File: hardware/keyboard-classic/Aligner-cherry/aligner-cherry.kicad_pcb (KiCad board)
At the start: 2 copper layers, 312.4 x 118.1 mm, 74 parts, among them SW1 RT Arrow, SW10 Bracket_Open, SW11 6, SW12 Y, SW13 Return, SW14 Dash, SW15 5, SW16 T, SW17 Line Feed, SW18 Colon, SW19 4, SW2 LT Arrow, SW20 R, SW21 O, SW22 0, SW23 3, SW24 E, SW25 L, SW26 9, SW27 2, SW28 W, SW29 Period, SW3 Tilde, SW30 8, SW31 1, SW32 @ (AT), SW33 Break, SW34 Rubout, SW35 R_Shift, SW36 P, SW37 Comma, SW38 K, SW39 L_Shift, SW4 I, SW40 Semicolon, SW41 M, SW42 J, SW43 Fwd_Slash, SW44 N, SW45 H, SW46 SPACE, SW47 B, SW48 G, SW49 TAB, SW5 Repeat, SW50 Z, SW51 V, SW52 F, SW53 CTRL, SW54 A, SW55 C, SW56 D, SW57 Backslash, SW58 Q, SW59 X, SW6 Bracket_Close, SW60 S, SW61 FN, SW62 ESC, SW7 7, SW8 U, SW9 Caps Lock

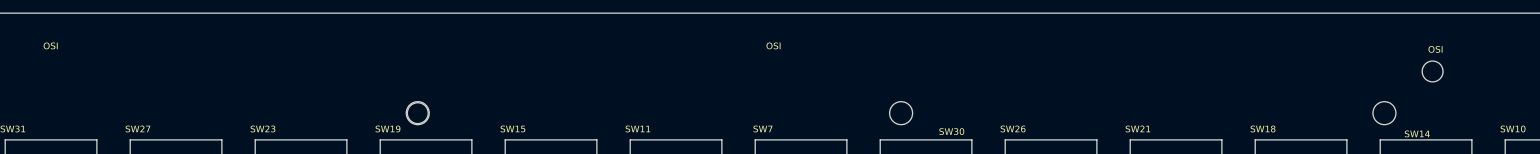
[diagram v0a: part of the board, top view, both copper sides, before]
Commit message: Replaced standard 20-pin header with header+mounting holes
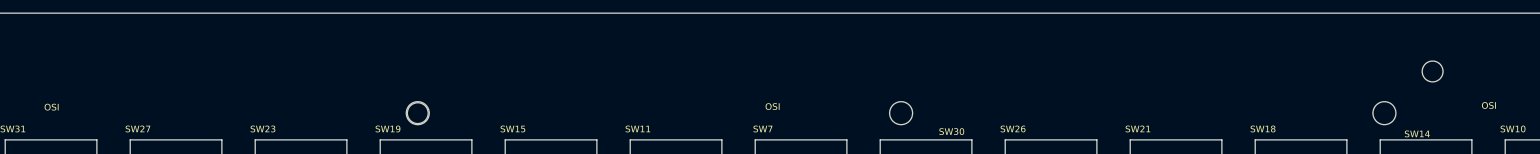
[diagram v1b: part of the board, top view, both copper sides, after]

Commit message: 0.05" adjustment to position of top mounting holes to match pcb
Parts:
- removed the REF** at (143.5, 78.7)
- removed the REF** at (364.5, 78.7)
- removed the REF** at (290.8, 78.7)
- added REF**: MountingHole_3.5mm, MountingHole:MountingHole_3.5mm, F.Cu at (143.5, 77.5)
- added REF**: MountingHole_3.5mm, MountingHole:MountingHole_3.5mm, F.Cu at (364.5, 77.5)
- added REF**: MountingHole_3.5mm, MountingHole:MountingHole_3.5mm, F.Cu at (290.8, 77.5)
- moved REF** 1.27 mm to (67.3, 77.5)
- moved REF** 1.27 mm to (217.2, 77.5)

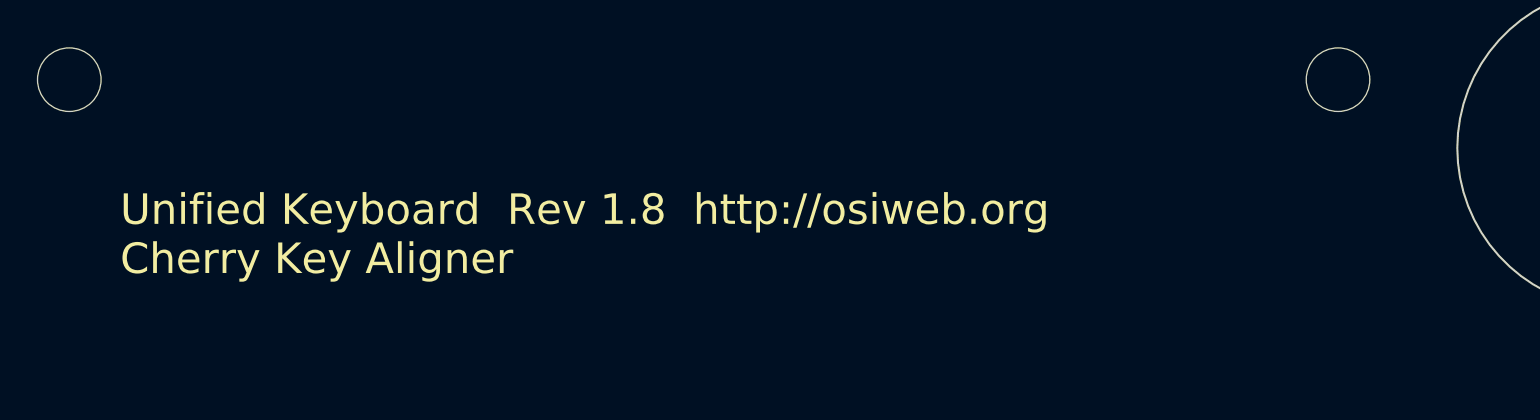
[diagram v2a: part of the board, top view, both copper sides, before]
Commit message: Add BOM parameter fields to apple2 and 328P encoders and classic kbd
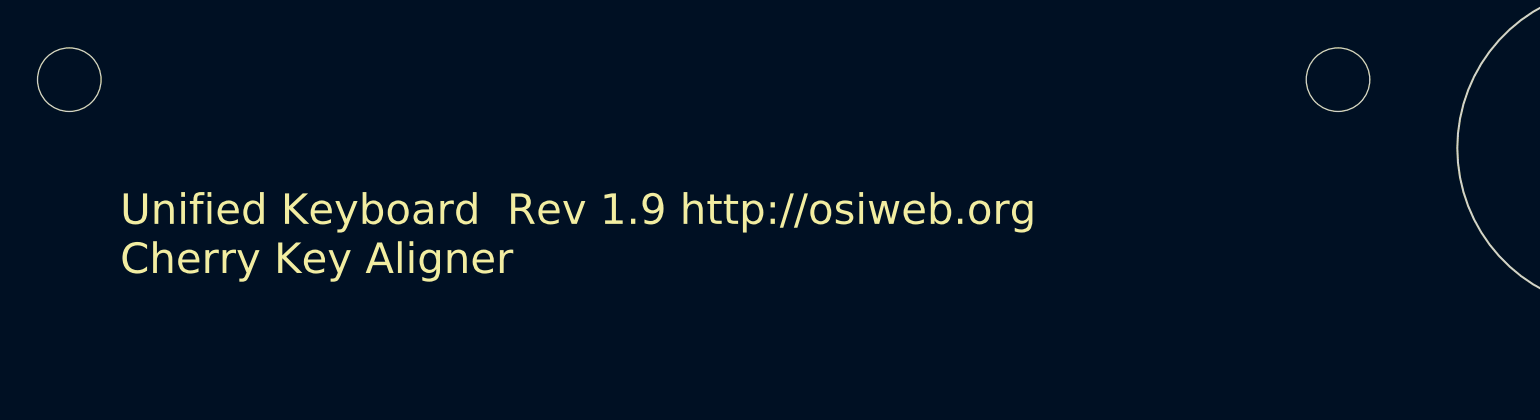
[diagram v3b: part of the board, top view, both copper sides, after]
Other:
- board text added: "Unified Keyboard Rev 1.9 http://osiweb.org Cherry Key Aligner"
- board text removed: "Unified Keyboard Rev 1.8 http://osiweb.org Cherry Key Aligner"

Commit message: Multiple fixes for keyboard PCB
- in combined CherryMX/futaba footprints, moved cherry pads down 1 mil and
futaba pads up 2 mil, to reduce risk of shortin of LED pads with futaba pad.
Adjusted all aligners accordingly

- Fixed centroid for combined diode footprint and adjusted PCB placement on
classic and SOL keyboards accordingly.

- Moved SMT pads in combined diode footprint to top layer, so pick & place file
will be usable.

- changes to futaba stabilizer design.  Longer post adapter passes through slots
in keyboard and aligner.

- Changed futaba post thickness gauge from board outline to a slot to improve
tolerance.

- Moved spacebar stabilizer bending guide to edge of PCB, in order to make it
more useful in bending PCBs.

- Changed Apple II mounting slots on classic keyboard from horizontal to
vertical orientation, to accommodate the different spacing offets due to the use
of spacers in angled mounting threads.
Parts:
- removed SW46: SPACE, unikbd:MX_space_aligner
- added REF**: MX_space_aligner, unikbd:MX_space_aligner, F.Cu at (197.2, 166.0)
- moved REF** 27.5 mm to (236.2, 177.8)
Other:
- outline, holes or cut-outs redrawn
- board text added: "Unified Keyboard Rev 1.10 http://osiweb.org Cherry Key Aligner"
- board text removed: "Stabilzer bend guide"
- board text removed: "Unified Keyboard Rev 1.9 http://osiweb.org Cherry Key Aligner"

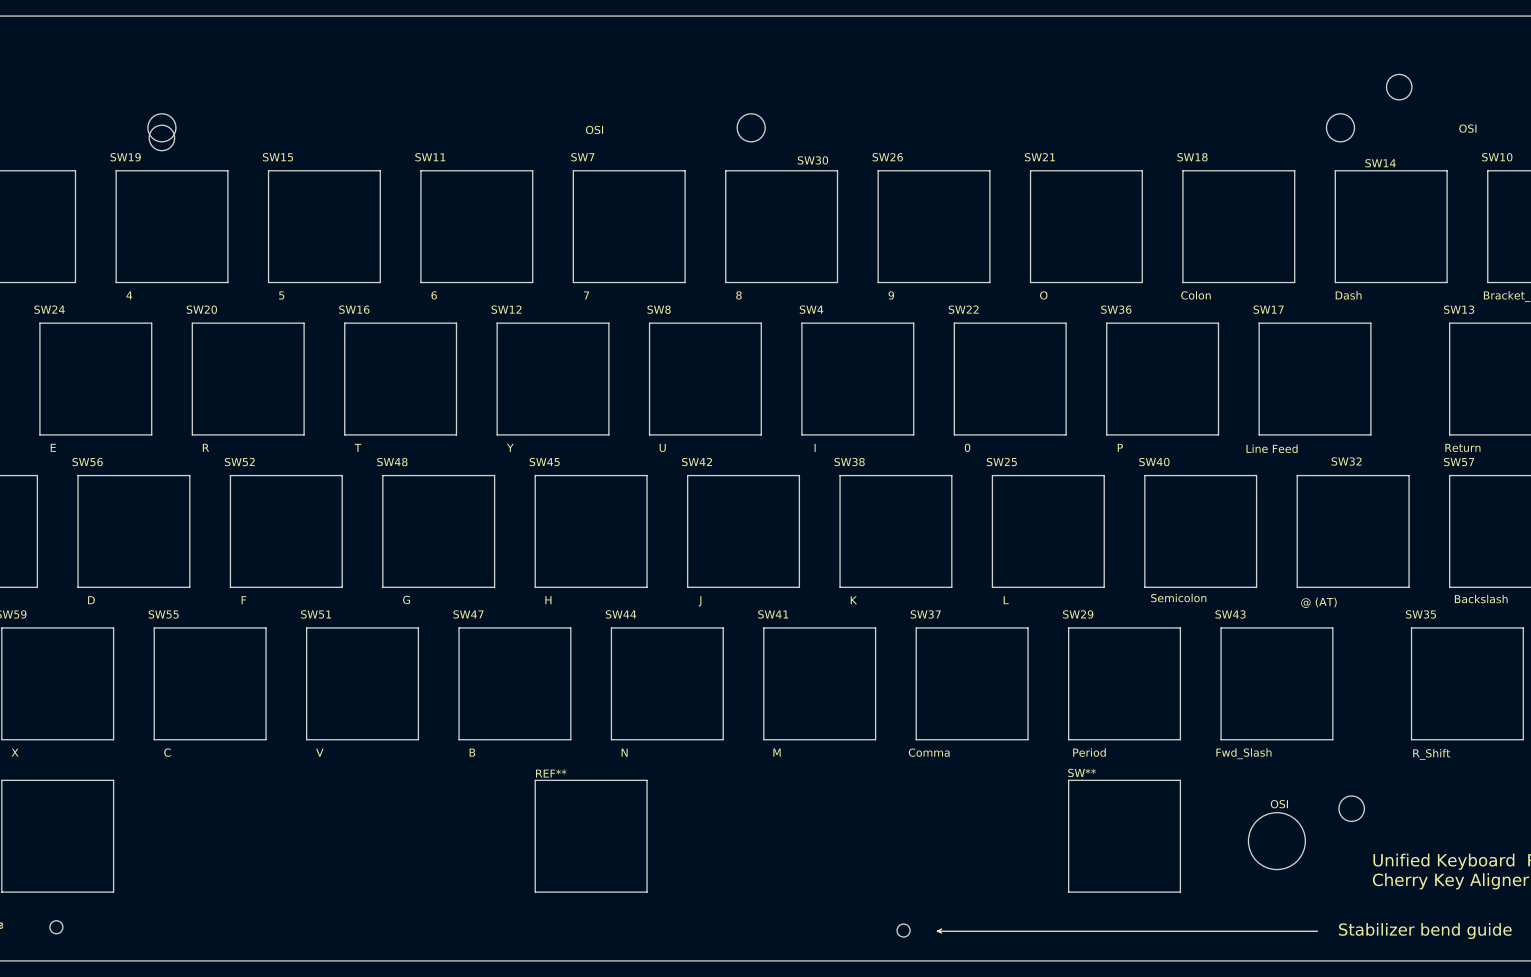
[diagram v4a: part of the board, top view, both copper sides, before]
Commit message: Apply fixes to cherry aligner.
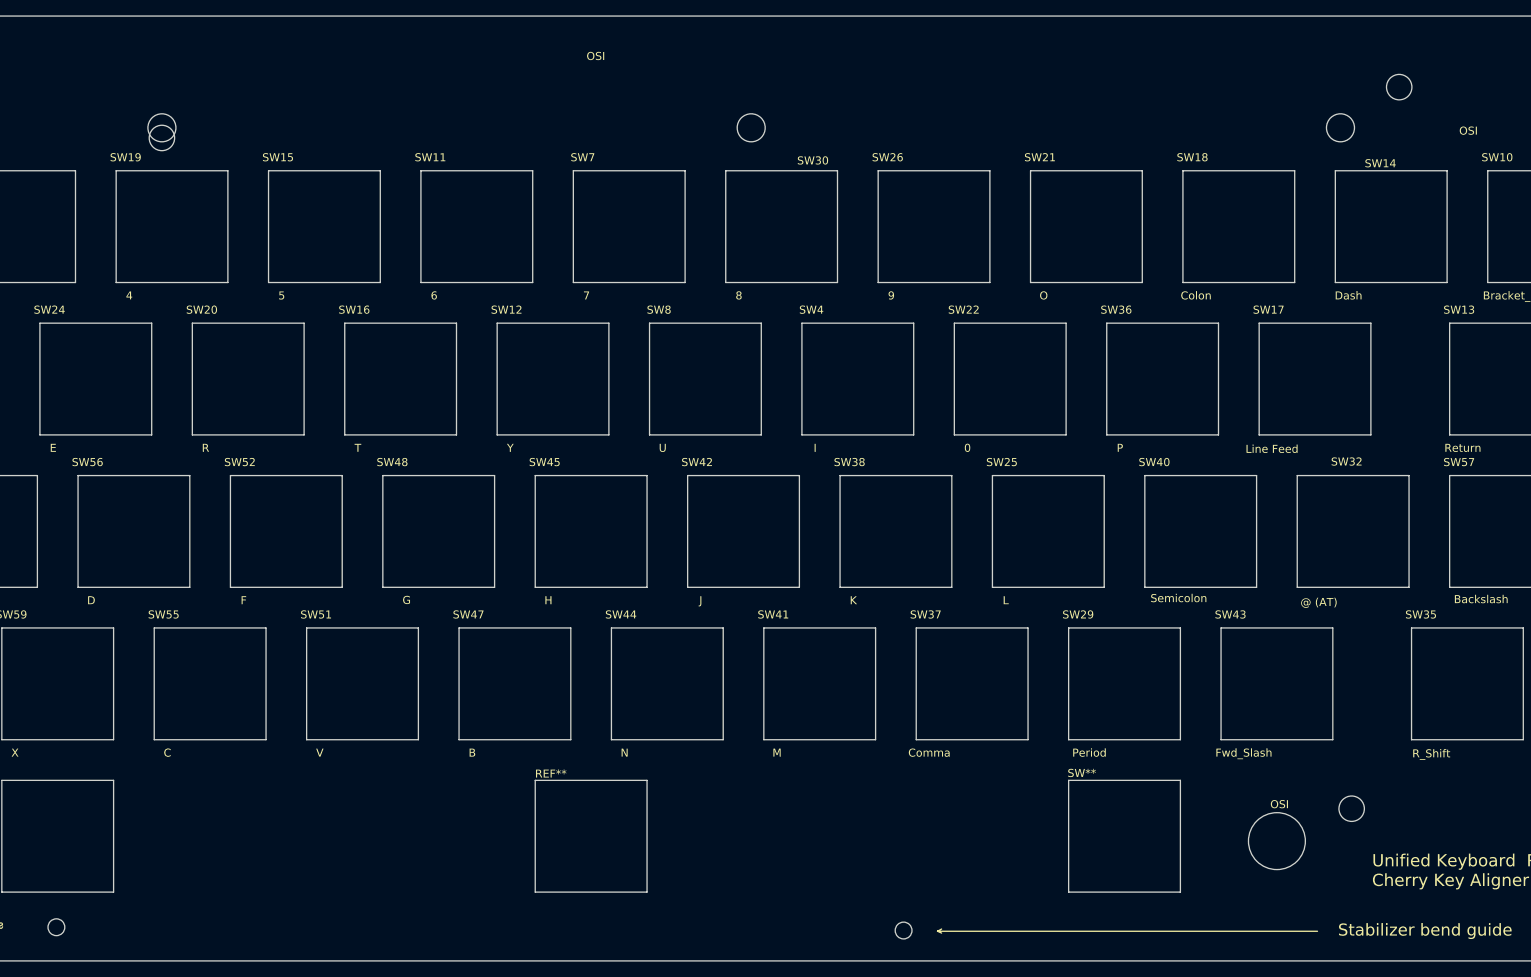
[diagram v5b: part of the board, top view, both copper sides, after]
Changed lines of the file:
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@@
+      (effects (font (size 1 1) (thickness 0.15)))
+    )
+    (fp_text user %R (at 110.75162 -87.97036) (layer F.Fab)
+      (effects (font (size 1 1) (thickness 0.15)))
+    )
+    (fp_text user OSI (at -109.4232 -88.138) (layer F.SilkS)
+      (effects (font (size 1 1) (thickness 0.15)))
+    )
+    (fp_text user %R (at -85.03158 5.42544) (layer F.Fab)
+      (effects (font (size 1 1) (thickness 0.15)))
+    )
+    (fp_text user OSI (at -85.28558 -4.17576) (layer F.SilkS)
+      (effects (font (size 1 1) (thickness 0.15)))
+    )
+    (fp_text user %R (at 86.31682 5.65404) (layer F.Fab)
+      (effects (font (size 1 1) (thickness 0.15)))
+    )
+    (fp_text user OSI (at 86.06282 -3.94716) (layer F.SilkS)
+      (effects (font (size 1 1) (thickness 0.15)))
+    )
+    (fp_text user OSI (at 0.59182 -97.46996) (layer F.SilkS)
+      (effects (font (size 1 1) (thickness 0.15)))
+    )
+    (fp_text user %R (at 0.84582 -87.86876) (layer F.Fab)
+      (effects (font (size 1 1) (thickness 0.15)))
+    )
+    (fp_text user OSI (at -109.4232 -88.138) (layer F.SilkS)
+      (effects (font (size 1 1) (thickness 0.15)))
+    )
+    (fp_text user %R (at -109.31398 -87.86876) (layer F.Fab)
+      (effects (font (size 1 1) (thickness 0.15)))
+    )
+    (fp_text user OSI (at 109.6772 -88.138) (layer F.SilkS)
+      (effects (font (size 1 1) (thickness 0.15)))
+    )
+    (fp_text user %R (at 110.75162 -87.97036) (layer F.Fab)
       (effects (font (size 1 1) (thickness 0.15)))
     )
@@
     (fp_circle (center -109.22 -92.71) (end -104.394 -92.71) (layer Cmts.User) (width 0.15))
     (fp_circle (center 109.22 -92.71) (end 114.046 -92.71) (layer Cmts.User) (width 0.15))
-    (fp_text user %R (at 110.75162 -87.97036) (layer F.Fab)
-      (effects (font (size 1 1) (thickness 0.15)))
-    )
-    (fp_text user OSI (at 109.6264 -88.392) (layer F.SilkS)
-      (effects (font (size 1 1) (thickness 0.15)))
-    )
-    (fp_text user %R (at -85.03158 5.42544) (layer F.Fab)
-      (effects (font (size 1 1) (thickness 0.15)))
-    )
-    (fp_text user OSI (at -85.28558 -4.17576) (layer F.SilkS)
-      (effects (font (size 1 1) (thickness 0.15)))
-    )
-    (fp_text user %R (at 86.31682 5.65404) (layer F.Fab)
-      (effects (font (size 1 1) (thickness 0.15)))
-    )
-    (fp_text user OSI (at 86.06282 -3.94716) (layer F.SilkS)
-      (effects (font (size 1 1) (thickness 0.15)))
-    )
-    (fp_text user OSI (at 0.45212 -88.22436) (layer F.SilkS)
-      (effects (font (size 1 1) (thickness 0.15)))
-    )
-    (fp_text user %R (at 0.84582 -87.86876) (layer F.Fab)
-      (effects (font (size 1 1) (thickness 0.15)))
-    )
-    (fp_text user OSI (at -109.4232 -88.138) (layer F.SilkS)
-      (effects (font (size 1 1) (thickness 0.15)))
-    )
-    (fp_text user %R (at -109.31398 -87.86876) (layer F.Fab)
-      (effects (font (size 1 1) (thickness 0.15)))
-    )
-    (fp_text user %R (at 110.75162 -87.97036) (layer F.Fab)
-      (effects (font (size 1 1) (thickness 0.15)))
-    )
     (pad "" np_thru_hole circle (at -85.725 0.635) (size 7.112 7.112) (drill 7.112) (layers *.Cu *.Mask))
     (pad "" np_thru_hole circle (at 85.725 0.635) (size 7.112 7.112) (drill 7.112) (layers *.Cu *.Mask))
@@
       (effects (font (size 1 1) (thickness 0.15)))
     )
-    (pad "" np_thru_hole circle (at 0 0) (size 1.6256 1.6256) (drill 1.6256) (layers *.Cu *.Mask))
+    (fp_text user %R (at 0.3 0) (layer F.Fab)
+      (effects (font (size 1 1) (thickness 0.15)))
+    )
+    (fp_circle (center 0 0) (end 2.1 0) (layer Cmts.User) (width 0.15))
+    (fp_circle (center 0 0) (end 2.35 0) (layer F.CrtYd) (width 0.05))
+    (pad "" np_thru_hole circle (at 0 0) (size 2.1 2.1) (drill 2.1) (layers *.Cu *.Mask))
   )
   (module MountingHole:MountingHole_2.1mm (layer F.Cu)
@@
       (effects (font (size 1 1) (thickness 0.15)))
     )
-    (pad "" np_thru_hole circle (at 0 0) (size 1.6256 1.6256) (drill 1.6256) (layers *.Cu *.Mask))
+    (fp_text user %R (at 0.3 0) (layer F.Fab)
+      (effects (font (size 1 1) (thickness 0.15)))
+    )
+    (fp_circle (center 0 0) (end 2.1 0) (layer Cmts.User) (width 0.15))
+    (fp_circle (center 0 0) (end 2.35 0) (layer F.CrtYd) (width 0.05))
+    (pad "" np_thru_hole circle (at 0 0) (size 2.1 2.1) (drill 2.1) (layers *.Cu *.Mask))
   )
   (module Symbol:OSHW-Logo2_9.8x8mm_SilkScreen (layer F.Cu)
@@
       (effects (font (size 1 1) (thickness 0.15)))
     )
-    (fp_circle (center 0 0) (end 3.5 0) (layer Cmts.User) (width 0.15))
-    (fp_circle (center 0 0) (end 3.75 0) (layer F.CrtYd) (width 0.05))
-    (fp_text user %R (at 0.3 0) (layer F.Fab) hide
-      (effects (font (size 1 1) (thickness 0.15)))
-    )
+    (fp_text user %R (at 0.3 0) (layer F.Fab) hide
+      (effects (font (size 1 1) (thickness 0.15)))
+    )
+    (fp_circle (center 0 0) (end 3.5 0) (layer Cmts.User) (width 0.15))
+    (fp_circle (center 0 0) (end 3.75 0) (layer F.CrtYd) (width 0.05))
     (pad 1 np_thru_hole circle (at 0 0) (size 3.5 3.5) (drill 3.5) (layers *.Cu *.Mask))
   )
@@
       (effects (font (size 1 1) (thickness 0.15)))
     )
-    (fp_circle (center 0 0) (end 3.75 0) (layer F.CrtYd) (width 0.05))
-    (fp_circle (center 0 0) (end 3.5 0) (layer Cmts.User) (width 0.15))
-    (fp_text user %R (at 0.3 0) (layer F.Fab) hide
-      (effects (font (size 1 1) (thickness 0.15)))
-    )
+    (fp_text user %R (at 0.3 0) (layer F.Fab) hide
+      (effects (font (size 1 1) (thickness 0.15)))
+    )
+    (fp_circle (center 0 0) (end 3.5 0) (layer Cmts.User) (width 0.15))
+    (fp_circle (center 0 0) (end 3.75 0) (layer F.CrtYd) (width 0.05))
     (pad 1 np_thru_hole circle (at 0 0) (size 3.5 3.5) (drill 3.5) (layers *.Cu *.Mask))
   )
@@
       (effects (font (size 1 1) (thickness 0.15)))
     )
-    (fp_circle (center 0 0) (end 3.75 0) (layer F.CrtYd) (width 0.05))
-    (fp_circle (center 0 0) (end 3.5 0) (layer Cmts.User) (width 0.15))
-    (fp_text user %R (at 0.3 0) (layer F.Fab) hide
-      (effects (font (size 1 1) (thickness 0.15)))
-    )
+    (fp_text user %R (at 0.3 0) (layer F.Fab) hide
+      (effects (font (size 1 1) (thickness 0.15)))
+    )
+    (fp_circle (center 0 0) (end 3.5 0) (layer Cmts.User) (width 0.15))
+    (fp_circle (center 0 0) (end 3.75 0) (layer F.CrtYd) (width 0.05))
     (pad 1 np_thru_hole circle (at 0 0) (size 3.5 3.5) (drill 3.5) (layers *.Cu *.Mask))
   )
@@
       (effects (font (size 1 1) (thickness 0.15)))
     )
-    (fp_circle (center 0 0) (end 3.75 0) (layer F.CrtYd) (width 0.05))
-    (fp_circle (center 0 0) (end 3.5 0) (layer Cmts.User) (width 0.15))
-    (fp_text user %R (at 0.3 0) (layer F.Fab) hide
-      (effects (font (size 1 1) (thickness 0.15)))
-    )
+    (fp_text user %R (at 0.3 0) (layer F.Fab) hide
+      (effects (font (size 1 1) (thickness 0.15)))
+    )
+    (fp_circle (center 0 0) (end 3.5 0) (layer Cmts.User) (width 0.15))
+    (fp_circle (center 0 0) (end 3.75 0) (layer F.CrtYd) (width 0.05))
     (pad 1 np_thru_hole circle (at 0 0) (size 3.5 3.5) (drill 3.5) (layers *.Cu *.Mask))
   )
@@
       (effects (font (size 1 1) (thickness 0.15)))
     )
-    (fp_circle (center 0 0) (end 3.75 0) (layer F.CrtYd) (width 0.05))
-    (fp_circle (center 0 0) (end 3.5 0) (layer Cmts.User) (width 0.15))
-    (fp_text user %R (at 0.3 0) (layer F.Fab) hide
-      (effects (font (size 1 1) (thickness 0.15)))
-    )
+    (fp_text user %R (at 0.3 0) (layer F.Fab) hide
+      (effects (font (size 1 1) (thickness 0.15)))
+    )
+    (fp_circle (center 0 0) (end 3.5 0) (layer Cmts.User) (width 0.15))
+    (fp_circle (center 0 0) (end 3.75 0) (layer F.CrtYd) (width 0.05))
     (pad 1 np_thru_hole circle (at 0 0) (size 3.5 3.5) (drill 3.5) (layers *.Cu *.Mask))
   )
@@
       (effects (font (size 1 1) (thickness 0.15)))
     )
-    (fp_circle (center 0 0) (end 3.75 0) (layer F.CrtYd) (width 0.05))
-    (fp_circle (center 0 0) (end 3.5 0) (layer Cmts.User) (width 0.15))
-    (fp_text user %R (at 0.3 0) (layer F.Fab) hide
-      (effects (font (size 1 1) (thickness 0.15)))
-    )
+    (fp_text user %R (at 0.3 0) (layer F.Fab) hide
+      (effects (font (size 1 1) (thickness 0.15)))
+    )
+    (fp_circle (center 0 0) (end 3.5 0) (layer Cmts.User) (width 0.15))
+    (fp_circle (center 0 0) (end 3.75 0) (layer F.CrtYd) (width 0.05))
     (pad 1 np_thru_hole circle (at 0 0) (size 3.5 3.5) (drill 3.5) (layers *.Cu *.Mask))
   )
@@
       (effects (font (size 1 1) (thickness 0.15)))
     )
-    (fp_circle (center 0 0) (end 3.75 0) (layer F.CrtYd) (width 0.05))
-    (fp_circle (center 0 0) (end 3.5 0) (layer Cmts.User) (width 0.15))
-    (fp_text user %R (at 0.3 0) (layer F.Fab) hide
-      (effects (font (size 1 1) (thickness 0.15)))
-    )
-    (pad 1 np_thru_hole circle (at 0 0) (size 3.5 3.5) (drill 3.5) (layers *.Cu *.Mask))
-  )
+    (fp_text user %R (at 0.3 0) (layer F.Fab) hide
+      (effects (font (size 1 1) (thickness 0.15)))
+    )
+    (fp_circle (center 0 0) (end 3.5 0) (layer Cmts.User) (width 0.15))
+    (fp_circle (center 0 0) (end 3.75 0) (layer F.CrtYd) (width 0.05))
+    (pad 1 np_thru_hole circle (at 0 0) (size 3.5 3.5) (drill 3.5) (layers *.Cu *.Mask))
+  )

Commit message: Moved Cherry MX and futaba pads farther apart in combined footprint
- Offset cherry MX pads and aligners downward 0.004" from origin

- Offset futaba pads and aligners upward -0.004" from origin

- Update footprints in classic and sol-20 pcbs and aligners

- adjust mounting slots in Sol-20 aligners to match futaba or cherry offset
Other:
- board text added: "Unified Keyboard Rev 1.11 http://osiweb.org Cherry Key Aligner"
- board text removed: "Unified Keyboard Rev 1.10 http://osiweb.org Cherry Key Aligner"
